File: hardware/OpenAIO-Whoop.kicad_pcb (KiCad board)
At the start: 6 copper layers, 30.3 x 30.3 mm, 249 parts, among them J1 U.FL, J10 M3, J13 M4, J2 +, J20 LED, J21 5V, J22 BZ-, J23 CAM, J24 5V, J25 GND, J26 VHD, J27 GND, J28 TX1, J29 RX1, J3 -, J31 USB, J32 CAM, J33 GND, J4 M1, J7 M2, Q26 AP1606, Q27 BC857BM, Q28 AP1606, Q29 AGM210MAP, Q30 AGM210MAP, Q31 AGM210MAP, Q32 AGM210MAP, Q33 AGM210MAP, Q34 AGM210MAP, Q35 AGM210MAP, Q36 AGM210MAP, Q37 AGM210MAP, Q38 AGM210MAP, Q39 AGM210MAP, Q40 AGM210MAP, SW1 SKUBAAE010, U1 INA186A3, U10 RP2354A, U11 BMI270, U12 TPS7A2018, U13 PY25Q128HA-DFH-IR, U14 SN74LVC1G3157, U15 TLV7031, U16 ESP32-PICO-V3, U18 SX1281, U19 RTC6705, U2 TPS61022, U20 SE5004L, U21 LP5912-3.3, U22 LP5907-2.85, U24 SGM40661, U3 TPS2116, U4 LP5912-3.3, U6 EFM8BB51F16I, U7 EFM8BB51F16I, U8 EFM8BB51F16I, U9 EFM8BB51F16I, X1 12MHz, X3 52MHz TCXO, X4 8MHz 10pF

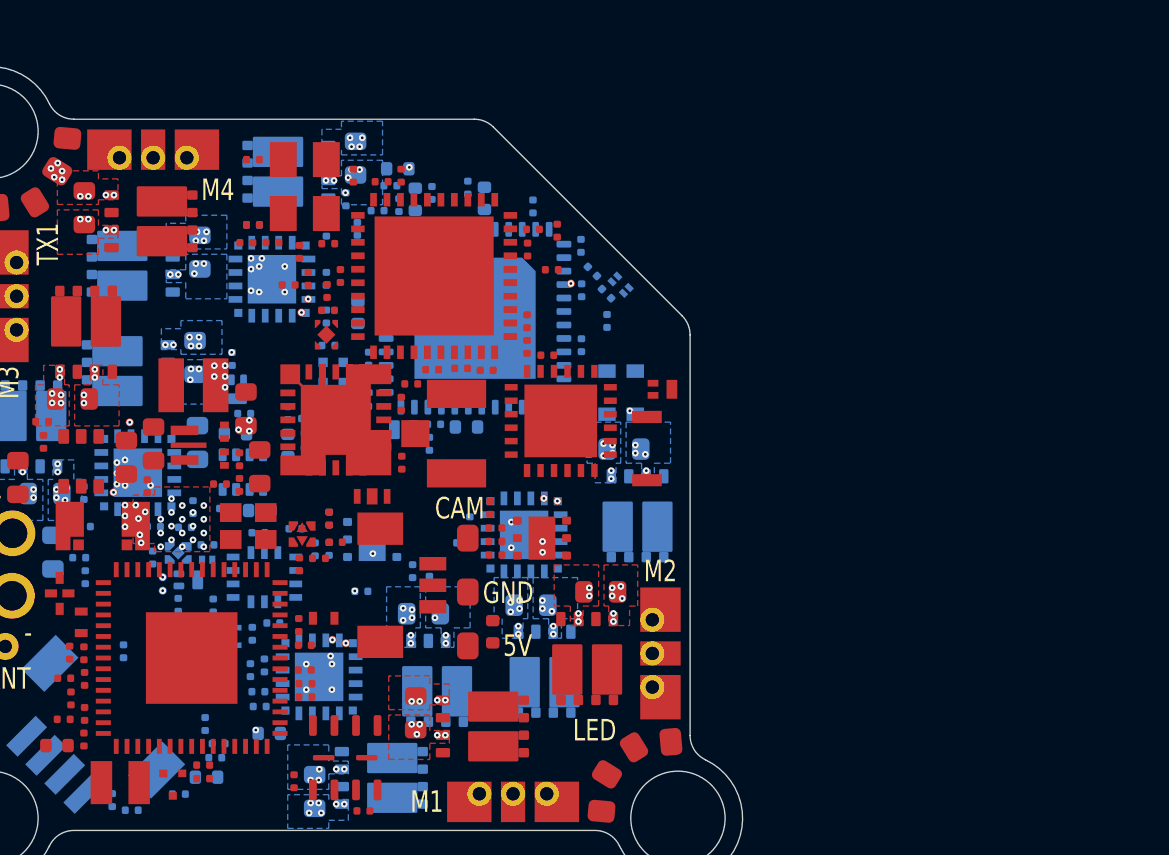
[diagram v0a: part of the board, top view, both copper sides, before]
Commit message: 5 V input: two Schottky diodes replace the TPS2116 mux and the SGM40661 (D118)
D9 VBUS -> +5V and D10 +5V_BST -> +5V, MSKSEMI MS2A40LDF DFN1610-2
(LCSC C7380000, imported with import_part.py; land spec PASS). U3, R7,
R8, U24, C131 removed; C128 is +5V bulk; PWR_FLAG on +5V. Board synced.

Stale schematic notes rewritten (O4 switch block now "HD_EN PULL-DOWN",
TVS, INA186 input RC, PA NTC, R67, GPIO4 control, root power table).

ERC 0 errors; check_netlist 7 ok; sch_integrate --check clean;
setup_board --check up to date; board_spec 31/31; sync dry run 0 changes;
DRC unchanged.

Co-Authored-By: Claude Opus 5.5 <noreply@anthropic.com>
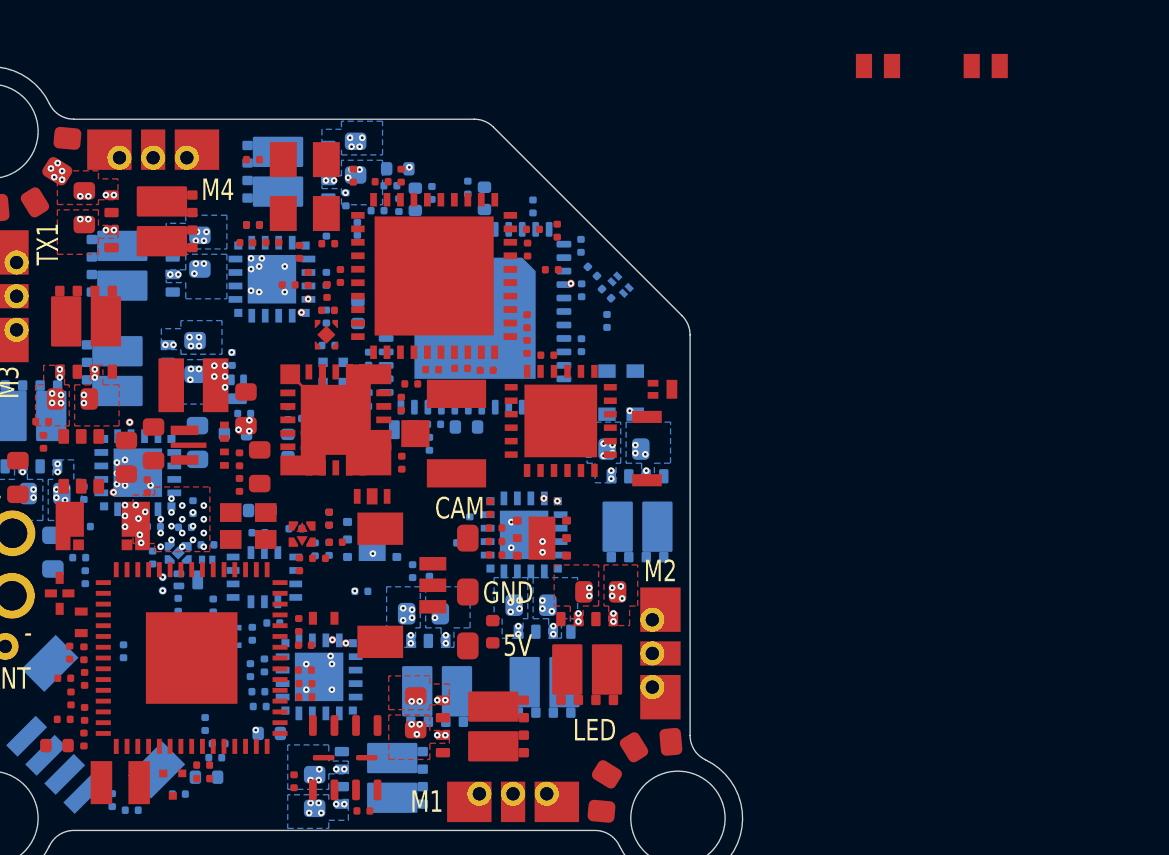
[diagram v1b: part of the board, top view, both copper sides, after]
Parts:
- removed C131: 100nF, lib:C_0201_0603Metric_L
- removed R7: 27.4k, lib:R_0201_0603Metric_L
- removed R8: 10k, lib:R_0201_0603Metric_L
- removed U24: SGM40661, lib:WLCSP-6_L1.30-W0.94-P0.40_SGM40661
- removed U3: TPS2116, lib:TI_SOT-583_DRL_L
- added D10: MS2A40LDF, lib:DFN1610-2_L1.6-W1.0-P1.05-RD, F.Cu at (133.4, 98.0)
- added D9: MS2A40LDF, lib:DFN1610-2_L1.6-W1.0-P1.05-RD, F.Cu at (137.4, 98.0)
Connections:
- C128 pad 1: +5V_USB -> +5V

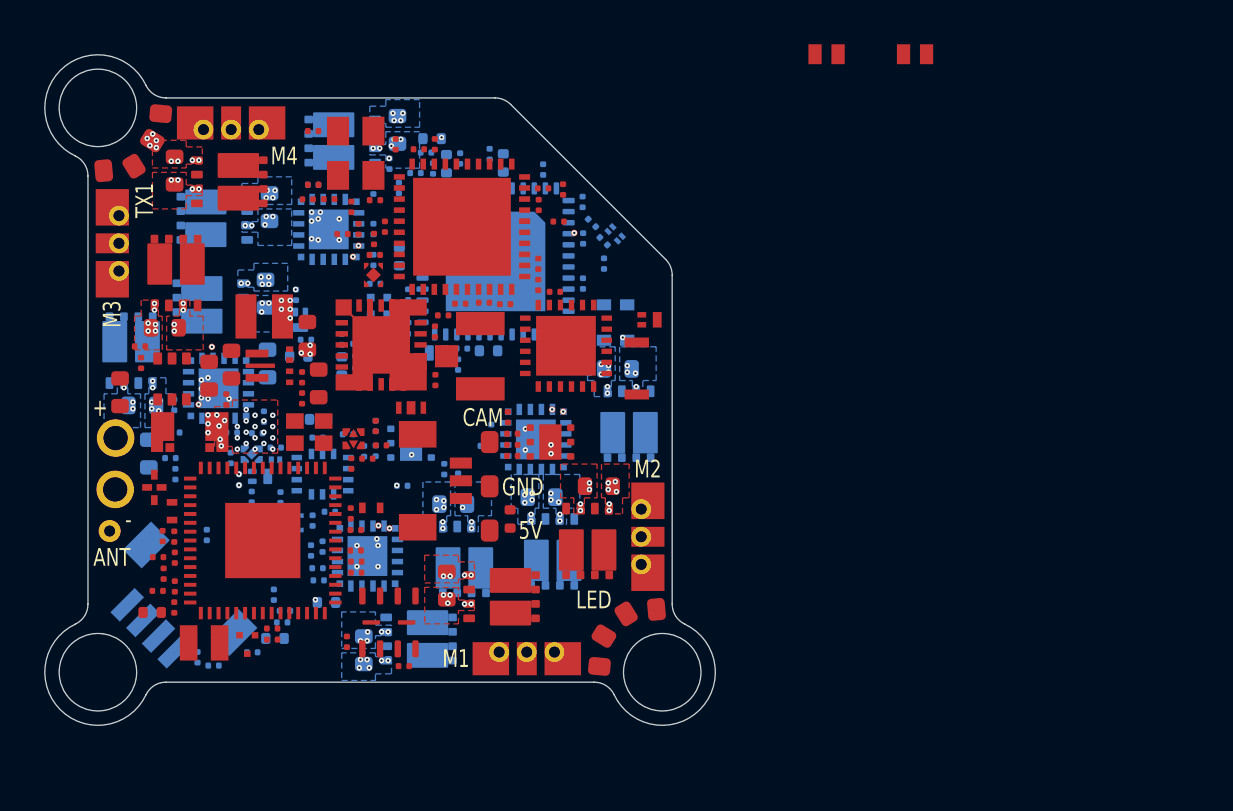
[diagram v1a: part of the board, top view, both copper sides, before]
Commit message: Board synced to the merged schematic, footprints refreshed from the library
sync_pcb: R89/R90/C135/C136 added, pads and test points to their new
footprints, R1 pins follow the flipped shunt. 131 footprints whose
library land changed (0201 pads 0.30 tall, J31/J33 overrides) replaced
from lib.pretty in place (position, rotation, side, lock and nets kept).
Remaining DRC is placement overlap from the larger pads (layout restart).

setup_board --check up to date; board_spec 31/31; sync dry run 0 changes.

Co-Authored-By: Claude Opus 5.5 <noreply@anthropic.com>
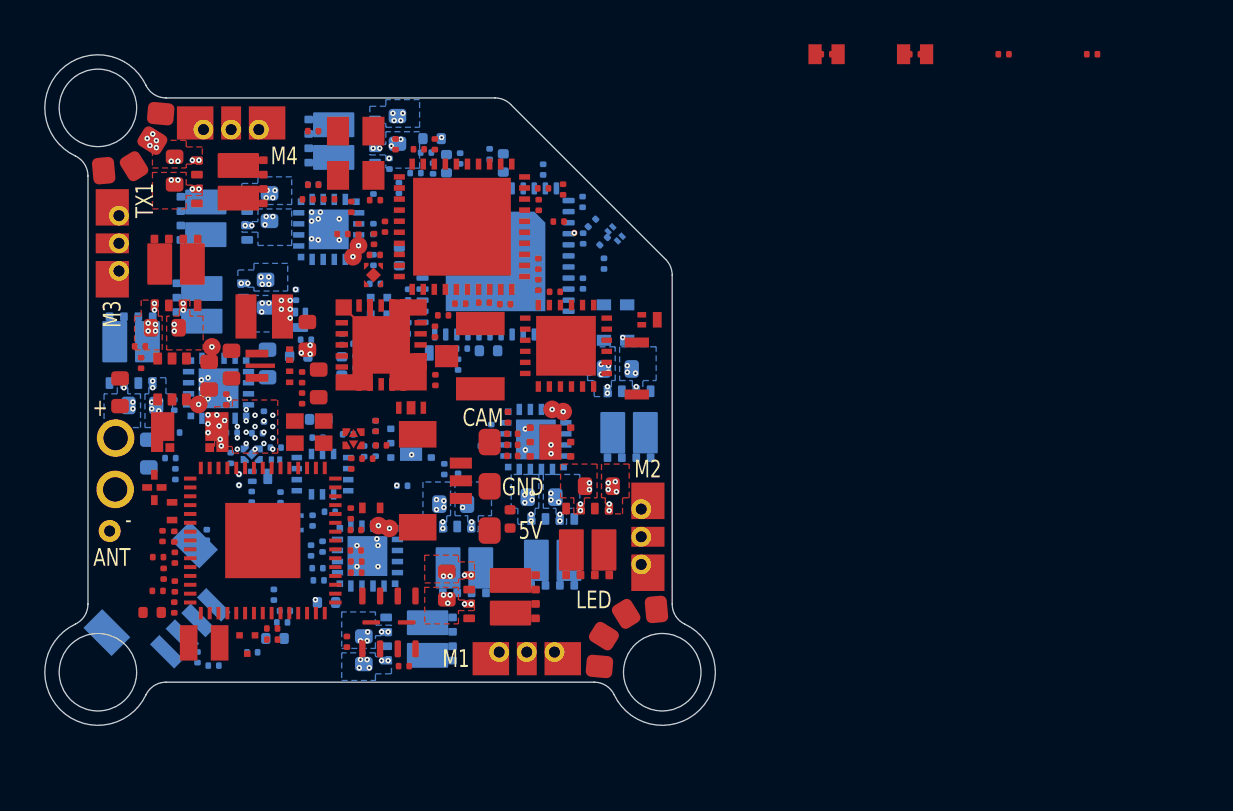
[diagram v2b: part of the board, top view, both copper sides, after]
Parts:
- added C135: 1uF, lib:C_0201_0603Metric_L, F.Cu at (133.4, 98.0)
- added C136: 1uF, lib:C_0201_0603Metric_L, F.Cu at (137.4, 98.0)
- added R89: 51R, lib:R_0201_0603Metric_L, F.Cu at (141.4, 98.0)
- added R90: 3.3k, lib:R_0201_0603Metric_L, F.Cu at (145.4, 98.0)
- J20, J21, J22, J23, J24, J25, J26, J27, J33: footprint lib:SolderPad_0.8x1.0mm -> lib:SolderPad_1.0x1.2mm
- J28: value TX1 -> TX0; footprint lib:SolderPad_0.8x1.0mm -> lib:SolderPad_1.0x1.2mm
- J29: value RX1 -> RX0; footprint lib:SolderPad_0.8x1.0mm -> lib:SolderPad_1.0x1.2mm
- TP1, TP2, TP3, TP4, TP5, TP6, TP7, TP8: footprint lib:TestPoint_Pad_D0.30mm_MicroVia_L -> lib:TestPoint_Pad_D0.8mm
- turned C102 to 90 degrees
- turned C104 to -90 degrees
- turned C109 to 90 degrees
- turned C112 to -90 degrees
- turned C116 to -90 degrees
- turned C117 to -90 degrees
- turned C125 to 90 degrees
- turned C132 to 45 degrees
- turned C133 to -90 degrees
- turned C25 to -90 degrees
- turned C37 to 90 degrees
- turned C42 to 90 degrees
- turned C47 to -90 degrees
- turned C50 to 90 degrees
- turned C51 to -90 degrees
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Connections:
- R1 pad 1: /POWER/CSA+ -> +BATT
- R1 pad 2: /POWER/SHUNT_SENSE_P -> /POWER/SHUNT_SENSE_N
- R1 pad 3: /POWER/SHUNT_SENSE_N -> /POWER/SHUNT_SENSE_P
- R1 pad 4: +BATT -> /POWER/CSA+
- U19 pad 17: unconnected-(U19-AVDD_6.5-Pad17) -> /VTX/U19_AVDD65
- U19 pad 40: +3.3V_VTX -> /VTX/U19_LDD2V5

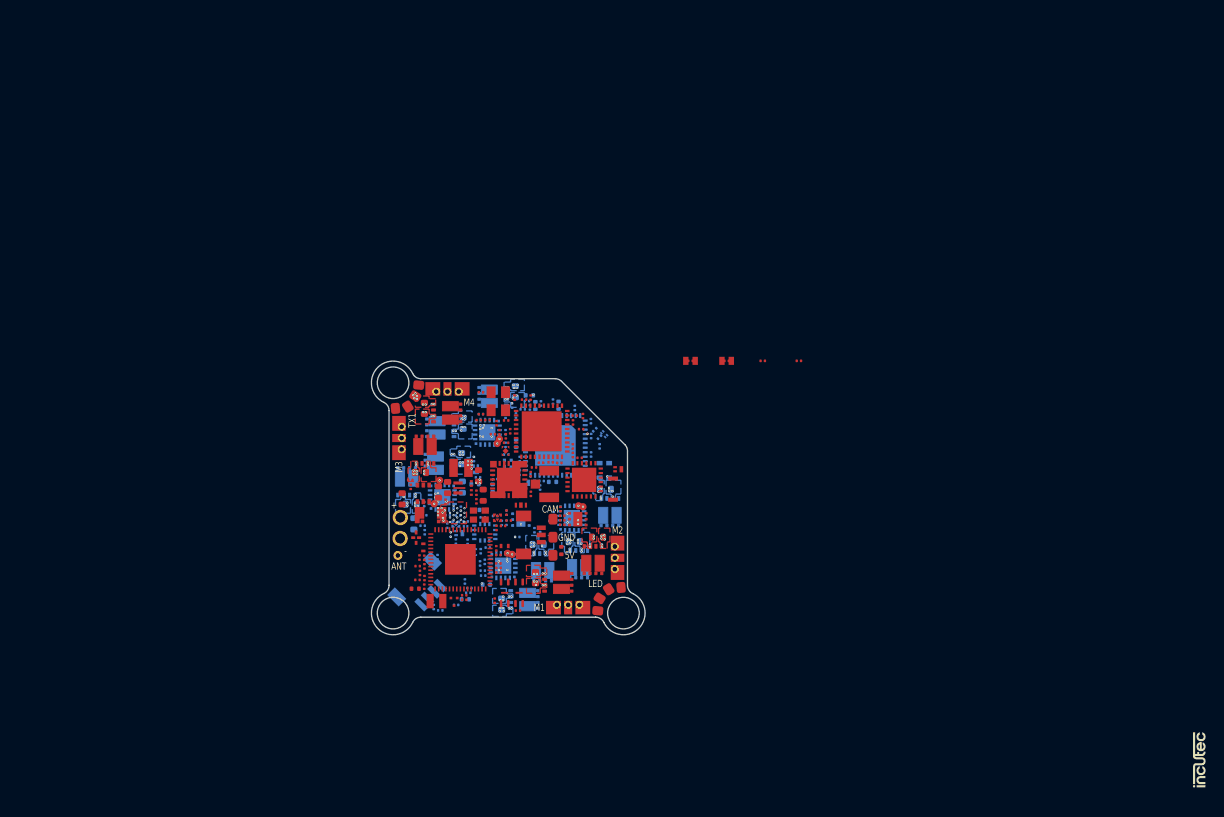
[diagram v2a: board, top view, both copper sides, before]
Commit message: Restore the owner's 13:39 board autosave, synced and set up for routing
Board from KiCad's project backup OpenAIO-Whoop-2026-10-11_133946.zip
(_autosave, the edits discarded at close): placement kept as the owner
left it. Then: sync_pcb (R89/R90/C135/C136 parked, solder pads and ESC
test pads to their new footprints, R1 nets), 131 footprints refreshed
from the library in place, the 24 rule areas and the L2_GND / L4_BATT /
L5_GND planes copied back from the last committed board (part-dependent
RF / Wi-Fi / shunt / boost areas sit at their old positions), and
setup_board for stackup, rules and outline. FET islands and the battery
feed pour are not restored (old FET placement).

setup_board --check up to date; board_spec 31/31; sync dry run 0 changes;
DRC parity 0; remaining DRC is placement overlap.

Co-Authored-By: Claude Opus 5.5 <noreply@anthropic.com>
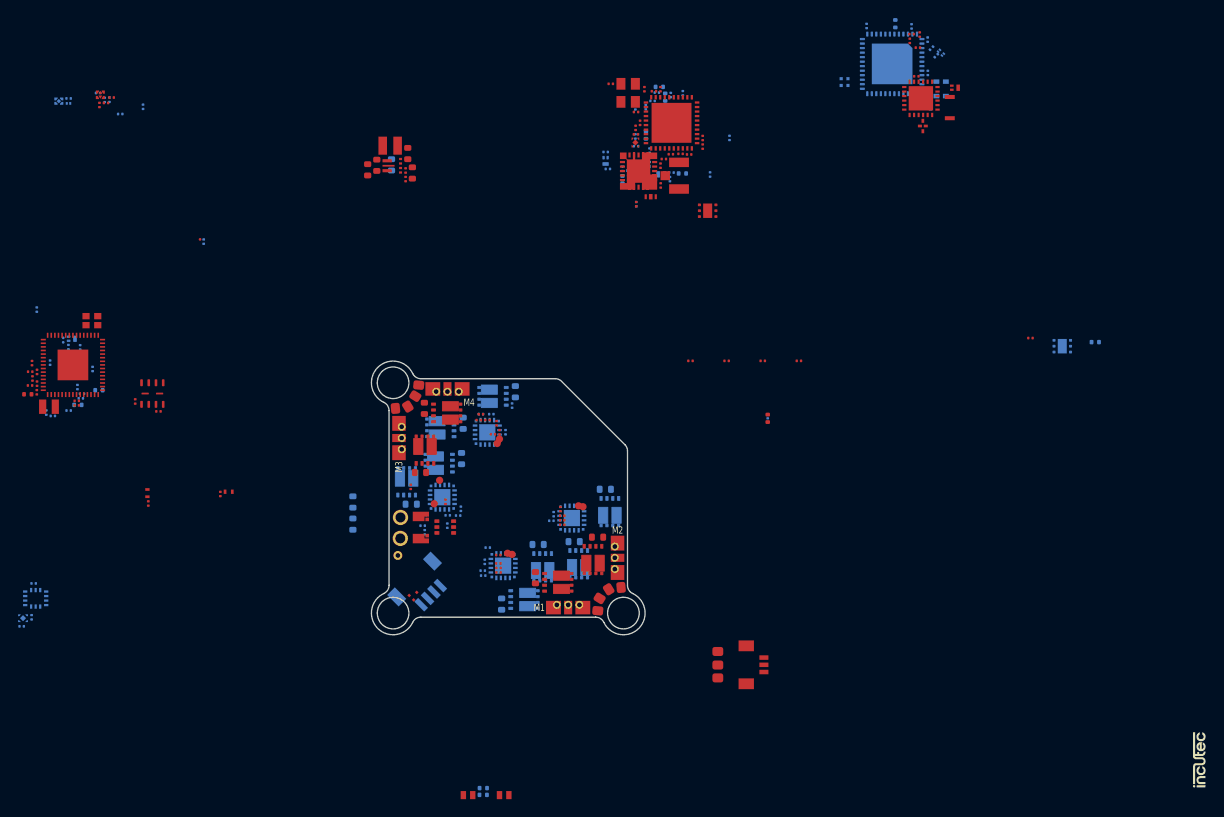
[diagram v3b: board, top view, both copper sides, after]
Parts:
- C1: moved to B.Cu
- moved FL1 72.3 mm to (159.1, 72.0)
- moved C13 70.4 mm to (178.2, 96.0)
- moved C14 70.4 mm to (171.0, 95.5)
- moved C66 64.2 mm to (69.0, 69.1)
- moved C67 64.2 mm to (70.2, 70.7)
- moved C68 64.2 mm to (64.5, 69.0)
- moved C70 64.2 mm to (67.8, 68.4)
- moved R51 64.2 mm to (69.3, 68.9)
- moved R52 64.2 mm to (67.9, 69.7)
- moved R53 64.2 mm to (68.7, 69.5)
- moved R54 64.2 mm to (68.5, 69.1)
- moved U14 64.2 mm to (68.0, 68.6)
- moved D3 64.2 mm to (64.5, 69.5)
- moved R55 64.2 mm to (72.8, 69.9)
- moved U15 64.2 mm to (63.4, 69.3)
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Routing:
- net GND: vias 123 -> 0
- net /RP2350A/SWDIO: vias 1 -> 0
- net /RP2350A/SWCLK: vias 1 -> 0
- net /FC_BOOT: vias 1 -> 0
- net /ESC4/C2D: vias 1 -> 0
- net /ESC4/C2CK: vias 1 -> 0
- net /ESC3/C2D: vias 1 -> 0
- net /ESC3/C2CK: vias 1 -> 0
- net /ESC2/C2D: vias 1 -> 0
- net /ESC2/C2CK: vias 1 -> 0
- net /ESC1/C2D: vias 1 -> 0
- net /ESC1/C2CK: vias 1 -> 0
- net +BATT: vias 178 -> 0
- removed copper zone on B.Cu, net +BATT
- removed copper zone on F.Cu, net +BATT
- removed copper zone on In1.Cu, net +BATT
- removed copper zone on In4.Cu, net +BATT
- removed copper zone on B.Cu, net GND
- removed copper zone on F.Cu, net GND
- removed copper zone on In2.Cu, net GND
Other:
- board text removed: "+"
- board text removed: "-"
- board text removed: "5V"
- board text removed: "ANT"
- board text removed: "ART [F]"
- board text removed: "BATT IN [B]"
- board text removed: "BATT IN [F]"
- board text removed: "BOOST 5 V [B]"
- board text removed: "BOOT [B]"
- board text removed: "BOOT [F]"
- board text removed: "CAM"
- board text removed: "CAM [F]"
- board text removed: "ESC1 [B]"
- board text removed: "ESC1 [F]"
- board text removed: "ESC2 [B]"
- board text removed: "ESC2 [F]"
- board text removed: "ESC3 [B]"
- board text removed: "ESC3 [F]"
- board text removed: "ESC4 [B]"
- board text removed: "ESC4 [F]"
- board text removed: "FC RP2354A [B]"
- board text removed: "FC RP2354A [F]"
- board text removed: "FC [F]"
- board text removed: "GND"
- board text removed: "HD PADS [F]"
- board text removed: "IMU [B]"
- board text removed: "IMU [F]"
- board text removed: "LED"
- board text removed: "LED [B]"
- board text removed: "LED [F]"
- board text removed: "LED/BZ PADS [F]"
- board text removed: "MUX + 3V3 [F]"
- board text removed: "NOR [F]"
- board text removed: "O4 SWITCH [B]"
- board text removed: "O4 SWITCH [F]"
- board text removed: "OPENAIO WHOOP"
- board text removed: "PIO OSD [B]"
- board text removed: "PIO OSD [F]"
- board text removed: "REV1"
- board text removed: "RX 2.4 GHz [F]"
- board text removed: "RX ESP32-PICO [B]"
- board text removed: "RX ESP32-PICO [F]"
- board text removed: "RX WIRE [F]"
- board text removed: "RX wire exit + frame path"
- board text removed: "SHUNT + INA [F]"
- board text removed: "TX1"
- board text removed: "U.FL coax (VTX antenna)"
- board text removed: "UART PADS [F]"
- board text removed: "USB"
- board text removed: "USB [B]"
- board text removed: "USB [F]"
- board text removed: "VTX PA / RF [B]"
- board text removed: "VTX PA / RF [F]"
- board text removed: "VTX PWR [B]"
- board text removed: "VTX PWR [F]"
- board text removed: "VTX RTC6705 [B]"
- board text removed: "VTX RTC6705 [F]"
- board text removed: "Wi-Fi ANT [B]"
- board text removed: "Wi-Fi ANT [F]"
- board text removed: "Wi-Fi antenna field"
